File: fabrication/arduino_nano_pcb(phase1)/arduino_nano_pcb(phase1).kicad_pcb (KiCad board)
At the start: 2 copper layers, 69.2 x 58 mm, 7 parts, among them J1 Conn_02x04_Odd_Even, J2 Conn_01x04_Pin

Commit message: feat(pcb_rev2): modified the pcb (rev 2)
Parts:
- H1: renamed from H4; footprint MountingHole:MountingHole_3.2mm_M3_Pad_TopBottom -> MountingHole:MountingHole_5mm_Pad_TopBottom
- H2: renamed from H3; footprint MountingHole:MountingHole_3.2mm_M3_Pad_TopBottom -> MountingHole:MountingHole_5mm_Pad_TopBottom
- H3: renamed from H2; footprint MountingHole:MountingHole_3.2mm_M3_Pad_TopBottom -> MountingHole:MountingHole_5mm_Pad_TopBottom
- H4: renamed from H1; footprint MountingHole:MountingHole_3.2mm_M3_Pad_TopBottom -> MountingHole:MountingHole_5mm_Pad_TopBottom
- J1: value Conn_02x04_Odd_Even -> Conn_01x04_Pin; footprint Connector_PinHeader_2.54mm:PinHeader_2x04_P2.54mm_Vertical -> Connector_PinHeader_2.54mm:PinHeader_1x04_P2.54mm_Horizontal
- J2: footprint Connector_PinHeader_2.54mm:PinHeader_1x04_P2.54mm_Vertical -> TM1637:TM1637
- moved J1 61.9 mm to (114.3, 86.1)
- moved A1 26.7 mm to (72.7, 82.3)
- moved J2 13.8 mm to (94.5, 63.3)
- moved H3 9.44 mm to (105.5, 72.0)
- moved H4 9.44 mm to (44.5, 72.0)
- moved H1 5.69 mm to (104.5, 109.0)
- moved H2 5.04 mm to (44.5, 109.0)
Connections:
- J1 pad 2: /MCU_RX_SENSOR_TX -> /MCU_TX_SENSOR_RX
- J1 pad 3: /MCU_TX_SENSOR_RX -> GND
- J1 pad 4: /MCU_TX_SENSOR_RX -> VCC
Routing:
- net VCC: track 84.9 -> 166.6 mm
- net /MCU_TX_SENSOR_RX: track 21.6 -> 80.4 mm
- net /MCU_RX_SENSOR_TX: track 25.4 -> 76.9 mm
- net /TM1637_DIO: track 22.0 -> 39.4 mm
- net /TM1637_CLK: track 26.2 -> 43.0 mm
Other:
- board size 69.2 x 58 mm -> 84 x 67.6 mm

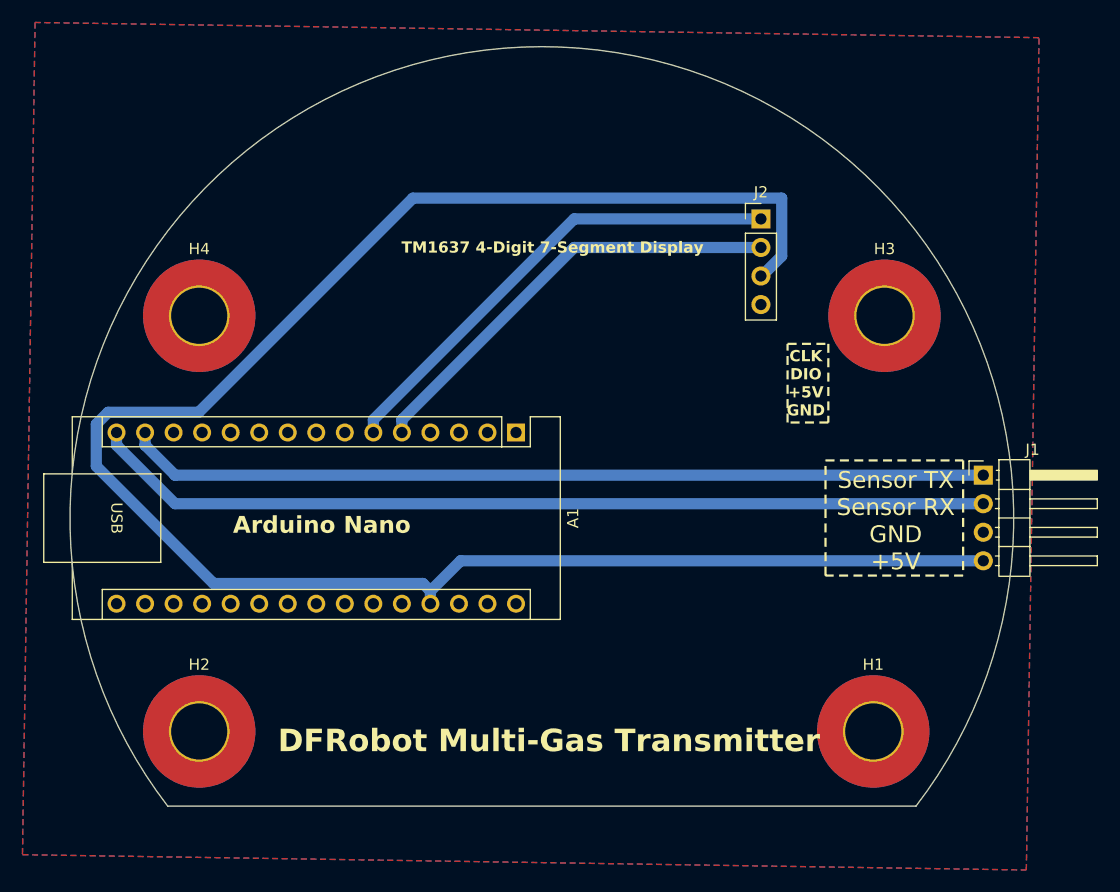
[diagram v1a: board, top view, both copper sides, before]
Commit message: fix(minor_footprint_fixes): minor fixes to tm1637 footprint
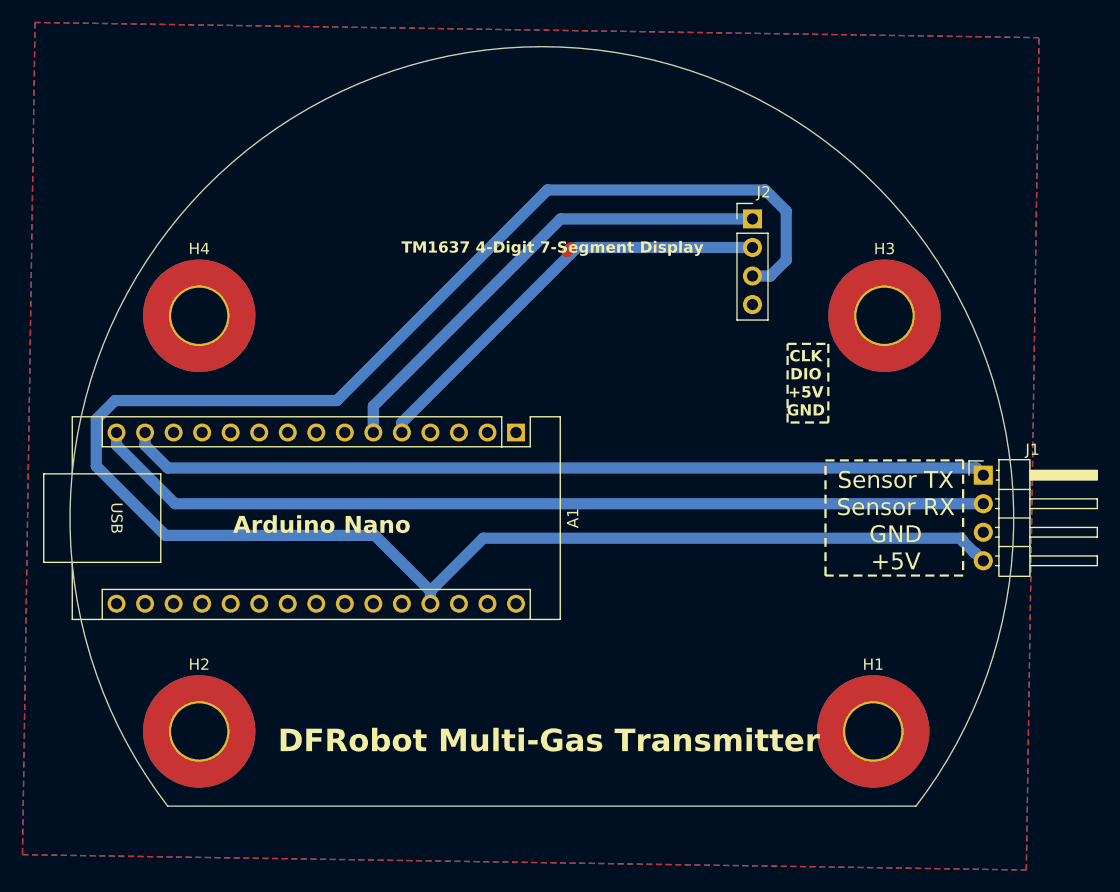
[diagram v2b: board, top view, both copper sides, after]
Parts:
- moved J2 0.25 mm to (94.8, 63.3)
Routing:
- net VCC: track 166.6 -> 170.3 mm
